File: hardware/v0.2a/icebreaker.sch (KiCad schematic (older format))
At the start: 114 parts, among them J1 Jumper, J10 Jumper, J11 Jumper, J12 Jumper, J13 Jumper, J14 Jumper, J15 Jumper, J16 Jumper, J17 Jumper, J18 Jumper, J19 Jumper, J2 Jumper, J20 Flash, J21 PMOD_1A, J22 PMOD_1B, J23 PMOD_2H, J24 PMOD_2P, J25 RGB Led, J26 5V AUX, J27 5V AUX, J3 Jumper, J4 Jumper, J5 Jumper, J6 Jumper, J7 Jumper, J8 Jumper, J9 Jumper, P1 pkl_USB_OTG, SW1 TACT, SW2 TACT, SW3 TACT, SW4 TACT, U1 93C46B-SOT-23-6, U2 3.3V, U3 1V2, U4 FT2232H, U5 W25Q, U6 ICE5LP4K-SG48, U7 12MHz

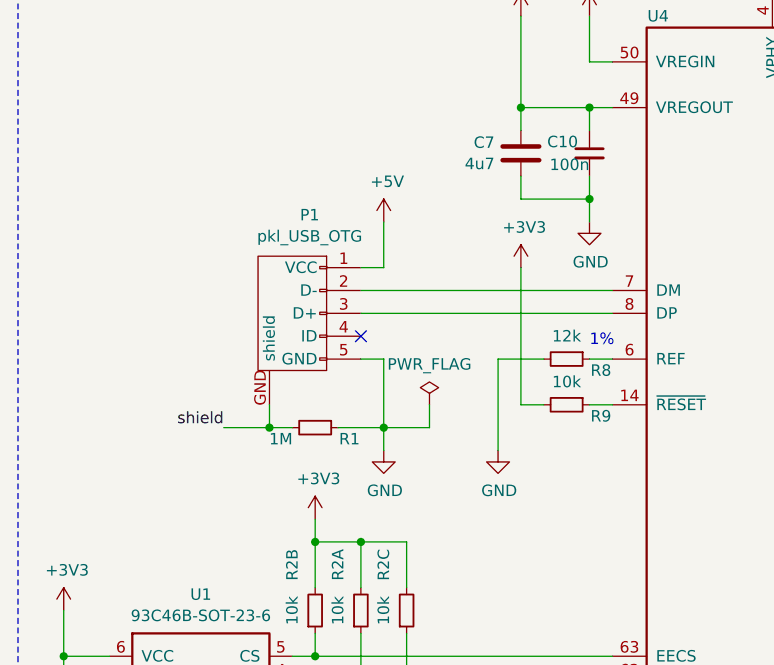
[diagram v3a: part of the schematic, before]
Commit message: Added USB signal pads.
These pads can be used for testing, debugging as well as hard wiring a
usb extension cable.
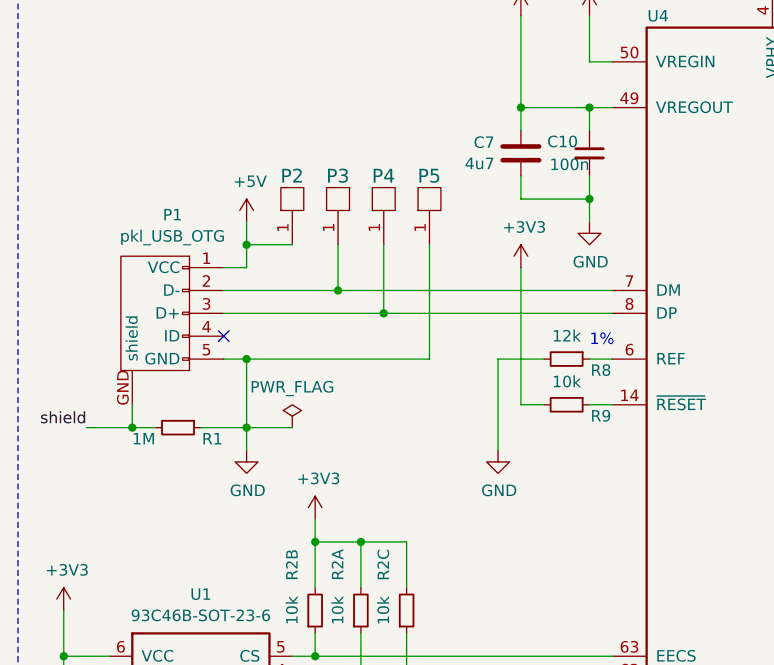
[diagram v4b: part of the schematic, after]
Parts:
- added P2, P3, P4, P5: UP, pkl_pads:PAD_SMD_1x2.65, symbol pkl_misc:PAD_SMD
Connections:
- net +5V: now also P2.1 (PAD)
- net GND: now also P5.1 (PAD)
- net at P1.2 (D-), U4.7 (DM): now also P3.1 (PAD)
- net at P1.3 (D+), U4.8 (DP): now also P4.1 (PAD)
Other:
- moved on the sheet: P1, R1
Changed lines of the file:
@@
 L pkl_conn:pkl_USB_OTG P1
 U 1 1 5A52ACD0
-P 1700 4350
-F 0 "P1" V 1270 4274 50  0000 C CNN
-F 1 "pkl_USB_OTG" V 1363 4274 50  0000 C CNN
-F 2 "pkl_connectors:Connector_USB_Micro_B_SMD" V 1355 4274 60  0001 C CNN
-F 3 "" V 1650 4250 60  0000 C CNN
-F 4 "ANY" H 1700 4350 50  0001 C CNN "Source"
-F 5 "conn-smd-usb-micro-b" H 0   0   50  0001 C CNN "Key"
-	1    1700 4350
+P 1100 4350
+F 0 "P1" V 670 4274 50  0000 C CNN
+F 1 "pkl_USB_OTG" V 763 4274 50  0000 C CNN
+F 2 "pkl_connectors:Connector_USB_Micro_B_SMD" V 755 4274 60  0001 C CNN
+F 3 "" V 1050 4250 60  0000 C CNN
+F 4 "ANY" H 1100 4350 50  0001 C CNN "Source"
+F 5 "conn-smd-usb-micro-b" H -600 0   50  0001 C CNN "Key"
+	1    1100 4350
 	0    -1   1    0
 $EndComp
 Wire Wire Line
-	2000 4250 3100 4250
+	1400 4250 1900 4250
 Wire Wire Line
-	2000 4350 3100 4350
-NoConn ~ 2000 4450
+	1400 4350 2100 4350
+NoConn ~ 1400 4450
 Wire Wire Line
-	2000 4550 2100 4550
+	1400 4550 1500 4550
 Wire Wire Line
-	2100 4550 2100 4850
+	1500 4550 1500 4850
 Wire Wire Line
-	1600 4750 1600 4850
+	1000 4750 1000 4850
 Wire Wire Line
-	1600 4850 1400 4850
-Text Label 1400 4850 2    50   ~ 0
+	1000 4850 800  4850
+Text Label 800  4850 2    50   ~ 0
 shield
 $Comp
 L pkl_device:pkl_R_Small R1
 U 1 1 5A52EC58
-P 1800 4850
-F 0 "R1" V 1850 5000 50  0000 C CNN
-F 1 "1M" V 1850 4700 50  0000 C CNN
-F 2 "pkl_dipol:R_0402" H 1859 4757 60  0001 L CNN
-F 3 "" H 1800 4850 60  0000 C CNN
-F 4 "ANY" H 1800 4850 50  0001 C CNN "Source"
-F 5 "res-0402-1m" H 0   0   50  0001 C CNN "Key"
-	1    1800 4850
+P 1200 4850
+F 0 "R1" V 1250 5000 50  0000 C CNN
+F 1 "1M" V 1250 4700 50  0000 C CNN
+F 2 "pkl_dipol:R_0402" H 1259 4757 60  0001 L CNN
+F 3 "" H 1200 4850 60  0000 C CNN
+F 4 "ANY" H 1200 4850 50  0001 C CNN "Source"
+F 5 "res-0402-1m" H -600 0   50  0001 C CNN "Key"
+	1    1200 4850
 	0    1    1    0
 $EndComp
 Wire Wire Line
-	1600 4850 1700 4850
-Connection ~ 1600 4850
+	1000 4850 1100 4850
+Connection ~ 1000 4850
 Wire Wire Line
-	1900 4850 2100 4850
+	1300 4850 1500 4850
 Wire Wire Line
-	2100 4850 2100 4950
-Connection ~ 2100 4850
+	1500 4850 1500 4950
+Connection ~ 1500 4850
 $Comp
 L power:GND #PWR06
 U 1 1 5A530D58
-P 2100 4950
-F 0 "#PWR06" H 2100 4700 50  0001 C CNN
-F 1 "GND" H 2105 4774 50  0000 C CNN
-F 2 "" H 2100 4950 50  0001 C CNN
-F 3 "" H 2100 4950 50  0001 C CNN
-	1    2100 4950
+P 1500 4950
+F 0 "#PWR06" H 1500 4700 50  0001 C CNN
+F 1 "GND" H 1505 4774 50  0000 C CNN
+F 2 "" H 1500 4950 50  0001 C CNN
+F 3 "" H 1500 4950 50  0001 C CNN
+	1    1500 4950
 	1    0    0    -1
 $EndComp
@@
 L power:PWR_FLAG #FLG01
 U 1 1 5A530EEE
-P 2300 4750
-F 0 "#FLG01" H 2300 4825 50  0001 C CNN
-F 1 "PWR_FLAG" H 2300 4927 50  0000 C CNN
-F 2 "" H 2300 4750 50  0001 C CNN
-F 3 "" H 2300 4750 50  0001 C CNN
-	1    2300 4750
+P 1700 4850
+F 0 "#FLG01" H 1700 4925 50  0001 C CNN
+F 1 "PWR_FLAG" H 1700 5027 50  0000 C CNN
+F 2 "" H 1700 4850 50  0001 C CNN
+F 3 "" H 1700 4850 50  0001 C CNN
+	1    1700 4850
 	1    0    0    -1
 $EndComp
 Wire Wire Line
-	2100 4850 2300 4850
-Wire Wire Line
-	2300 4850 2300 4750
+	1500 4850 1700 4850
 Wire Wire Line
 	3100 3250 3000 3250
@@
 $EndComp
 Wire Wire Line
-	2000 4150 2100 4150
-Wire Wire Line
-	2100 4150 2100 3950
+	1400 4150 1500 4150
 $Comp
 L power:+5V #PWR08
 U 1 1 5A5336DE
-P 2100 3950
-F 0 "#PWR08" H 2100 3800 50  0001 C CNN
-F 1 "+5V" H 2115 4126 50  0000 C CNN
-F 2 "" H 2100 3950 50  0001 C CNN
-F 3 "" H 2100 3950 50  0001 C CNN
-	1    2100 3950
+P 1500 3950
+F 0 "#PWR08" H 1500 3800 50  0001 C CNN
+F 1 "+5V" H 1515 4126 50  0000 C CNN
+F 2 "" H 1500 3950 50  0001 C CNN
+F 3 "" H 1500 3950 50  0001 C CNN
+	1    1500 3950
 	1    0    0    -1
 $EndComp
@@
 Text Label 12500 5700 2    25   ~ 0
 P2_4x
+$Comp
+L pkl_misc:PAD_SMD P2
+U 1 1 5D27BE59
+P 1700 3850
+F 0 "P2" V 1800 3800 60  0000 L CNN
+F 1 "UP" H 1650 3950 60  0001 L CNN
+F 2 "pkl_pads:PAD_SMD_1x2.65" H 1700 3600 60  0001 C CNN
+F 3 "" H 1700 3700 60  0000 C CNN
+F 4 "ANY" H 1700 3850 50  0001 C CNN "Source"
+	1    1700 3850
+	0    -1   -1   0
+$EndComp
+Connection ~ 1900 4250
+Wire Wire Line
+	1900 4250 3100 4250
+Wire Wire Line
+	1900 4050 1900 4250
+Wire Wire Line
+	1500 3950 1500 4050
+Wire Wire Line
+	1700 4050 1500 4050
+Connection ~ 1500 4050
+Wire Wire Line
+	1500 4050 1500 4150
+Wire Wire Line
+	2100 4050 2100 4350
+Connection ~ 2100 4350
+Wire Wire Line
+	2100 4350 3100 4350
+Wire Wire Line
+	2300 4050 2300 4550
+Wire Wire Line
+	2300 4550 1500 4550
+Connection ~ 1500 4550
+$Comp
+L pkl_misc:PAD_SMD P3
+U 1 1 5D620E4E
+P 1900 3850
+F 0 "P3" V 2000 3800 60  0000 L CNN
+F 1 "UP" H 1850 3950 60  0001 L CNN
+F 2 "pkl_pads:PAD_SMD_1x2.65" H 1900 3600 60  0001 C CNN
+F 3 "" H 1900 3700 60  0000 C CNN
+F 4 "ANY" H 1900 3850 50  0001 C CNN "Source"
+	1    1900 3850
+	0    -1   -1   0
+$EndComp
+$Comp
+L pkl_misc:PAD_SMD P4
+U 1 1 5D620F84
+P 2100 3850
+F 0 "P4" V 2200 3800 60  0000 L CNN
+F 1 "UP" H 2050 3950 60  0001 L CNN
+F 2 "pkl_pads:PAD_SMD_1x2.65" H 2100 3600 60  0001 C CNN
+F 3 "" H 2100 3700 60  0000 C CNN
+F 4 "ANY" H 2100 3850 50  0001 C CNN "Source"
+	1    2100 3850
+	0    -1   -1   0
+$EndComp
+$Comp
+L pkl_misc:PAD_SMD P5
+U 1 1 5D6210C0
+P 2300 3850
+F 0 "P5" V 2400 3800 60  0000 L CNN
+F 1 "UP" H 2250 3950 60  0001 L CNN
+F 2 "pkl_pads:PAD_SMD_1x2.65" H 2300 3600 60  0001 C CNN
+F 3 "" H 2300 3700 60  0000 C CNN
+F 4 "ANY" H 2300 3850 50  0001 C CNN "Source"
+	1    2300 3850
+	0    -1   -1   0
+$EndComp
 $EndSCHEMATC

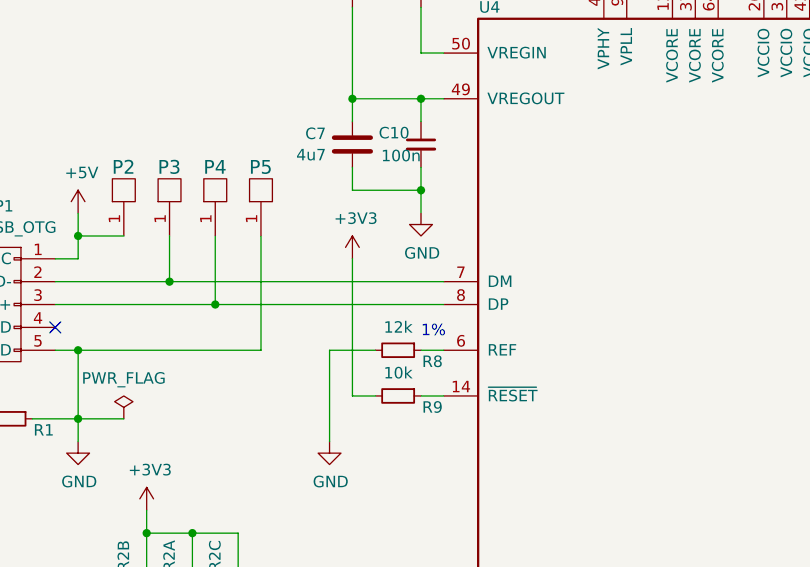
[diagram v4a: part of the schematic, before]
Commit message: Improved silkscreen legend for more intutive usage.
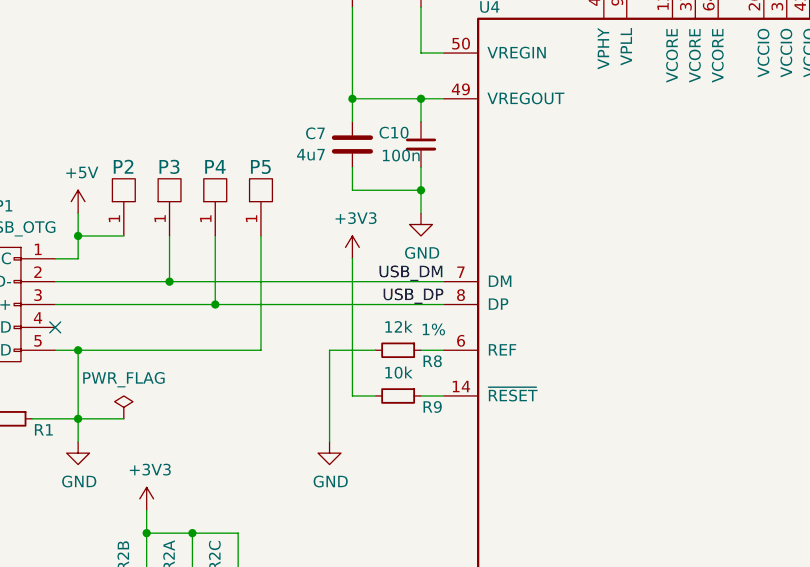
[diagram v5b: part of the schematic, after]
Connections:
- net USB_DM: now reaches P1.2 (D-), P3.1 (PAD), U4.7 (DM)
- net USB_DP: now reaches P1.3 (D+), P4.1 (PAD), U4.8 (DP)
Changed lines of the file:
@@
 	0    -1   -1   0
 $EndComp
+Text Label 3100 4250 2    50   ~ 0
+USB_DM
+Text Label 3100 4350 2    50   ~ 0
+USB_DP
 $EndSCHEMATC

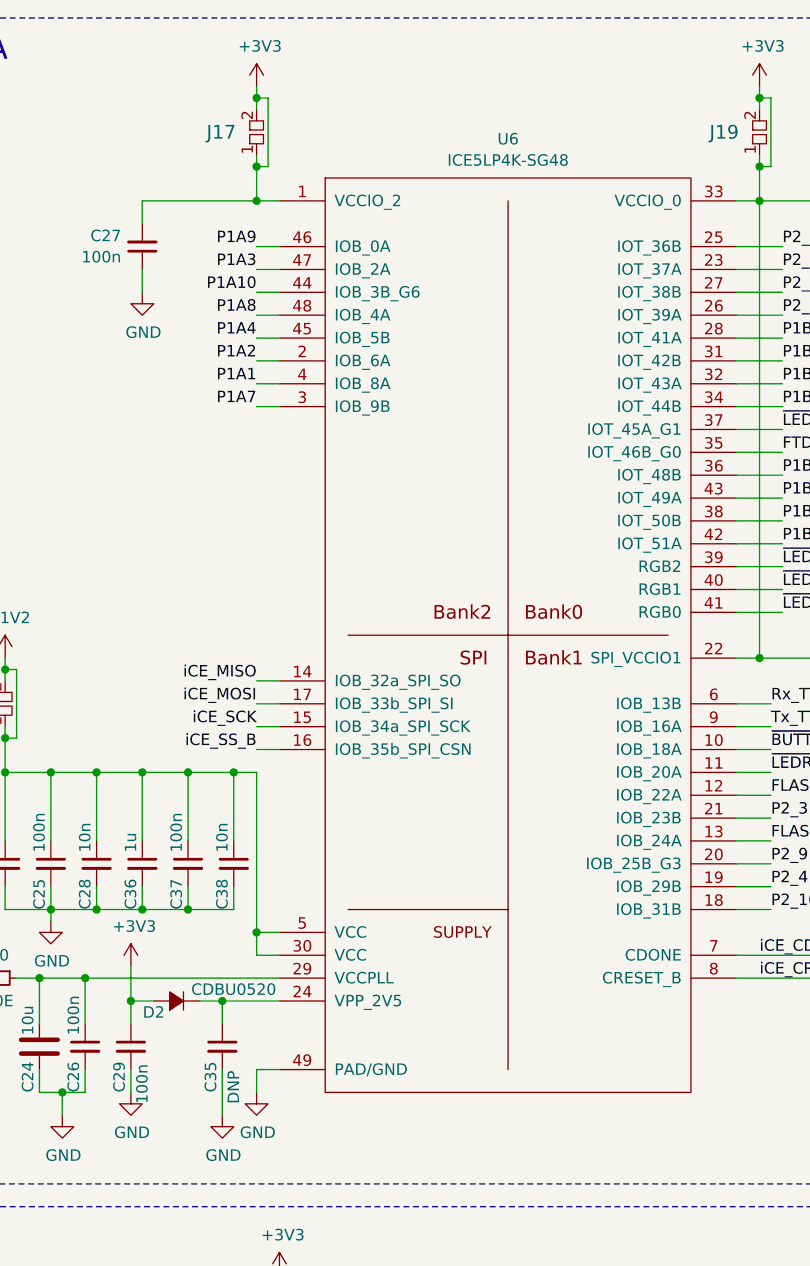
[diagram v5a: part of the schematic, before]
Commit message: Fixed pin header 3d models.
We had some of the models doubled up or not fully disabled. Now the TH
pin headers are all using KiCad V5 3d model locations and are all
disabled.

This fixes #23
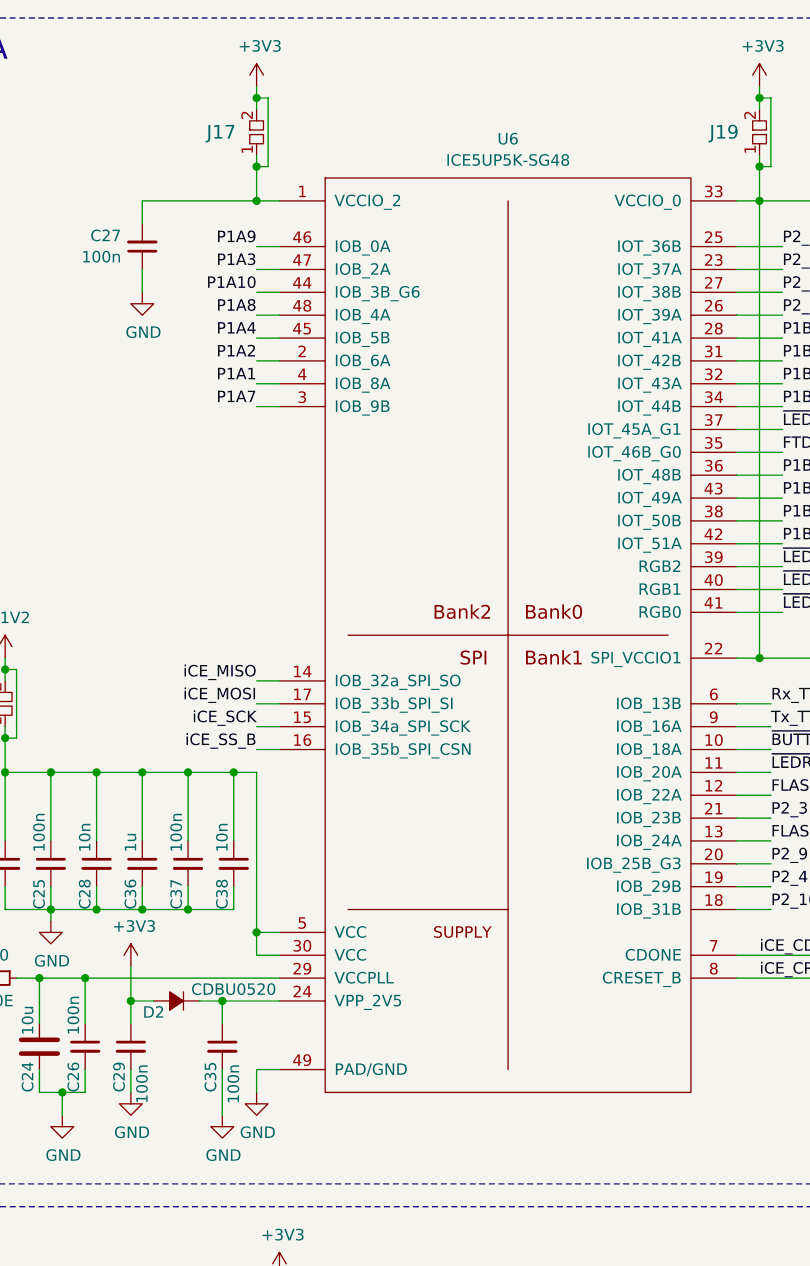
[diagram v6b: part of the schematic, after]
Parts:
- C35: value DNP -> 100n; Key (none) -> cap-cer-100n
- C6, C7, C9: Key cap-cer-0402-4u7 -> cap-cer-0603-4u7
- D2: Key diode-shottky-0603 -> diode-schottky-0603
- U6: value ICE5LP4K-SG48 -> ICE5UP5K-SG48; Key ic-ice5lp4k-sg48 -> ic-ice5up5k-sg48
- U7: Key (none) -> xtal-sot23-5-12mhz-osc
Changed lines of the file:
@@
 P 9600 4200
 F 0 "U6" H 9600 6370 50  0000 C CNN
-F 1 "ICE5LP4K-SG48" H 9600 6277 50  0000 C CNN
+F 1 "ICE5UP5K-SG48" H 9600 6277 50  0000 C CNN
 F 2 "pkl_housings_dfn_qfn:QFN-48-1EP_7x7mm_Pitch0.5mm" H 11900 4400 50  0001 C CNN
 F 3 "" H 11900 4400 50  0001 C CNN
-F 4 "ANY" H 9600 4200 50  0001 C CNN "Source"
-F 5 "ic-ice5lp4k-sg48" H 0   0   50  0001 C CNN "Key"
+F 4 "ic-ice5up5k-sg48" H 0   0   50  0001 C CNN "Key"
+F 5 "ANY" H 9600 4200 50  0001 C CNN "Source"
 	1    9600 4200
 	1    0    0    -1
@@
 F 2 "pkl_dipol:C_0603" H 3092 2357 60  0001 L CNN
 F 3 "" H 3000 2450 60  0000 C CNN
-F 4 "cap-cer-0402-4u7" H 0   0   50  0001 C CNN "Key"
+F 4 "cap-cer-0603-4u7" H 0   0   50  0001 C CNN "Key"
 F 5 "ANY" H 3000 2450 50  0001 C CNN "Source"
 	1    3000 2450
@@
 F 2 "pkl_dipol:C_0603" H 2792 2357 60  0001 L CNN
 F 3 "" H 2700 2450 60  0000 C CNN
-F 4 "cap-cer-0402-4u7" H 0   0   50  0001 C CNN "Key"
+F 4 "cap-cer-0603-4u7" H 0   0   50  0001 C CNN "Key"
 F 5 "ANY" H 2700 2450 50  0001 C CNN "Source"
 	1    2700 2450
@@
 F 2 "pkl_dipol:D_0603" V 8150 5800 60  0001 C CNN
 F 3 "" V 8150 5800 60  0000 C CNN
-F 4 "ANY" H 8150 5800 50  0001 C CNN "Source"
-F 5 "diode-shottky-0603" H 0   0   50  0001 C CNN "Key"
+F 4 "diode-schottky-0603" H 0   0   50  0001 C CNN "Key"
+F 5 "ANY" H 8150 5800 50  0001 C CNN "Source"
 	1    8150 5800
 	1    0    0    -1
@@
 F 2 "pkl_dipol:C_0603" H 2792 3557 60  0001 L CNN
 F 3 "" H 2700 3650 60  0000 C CNN
-F 4 "cap-cer-0402-4u7" H 0   0   50  0001 C CNN "Key"
+F 4 "cap-cer-0603-4u7" H 0   0   50  0001 C CNN "Key"
 F 5 "ANY" H 2700 3650 50  0001 C CNN "Source"
 	1    2700 3650
@@
 P 8350 6000
 F 0 "C35" V 8400 5800 50  0000 L CNN
-F 1 "DNP" V 8300 5750 50  0000 L CNN
+F 1 "100n" V 8300 5750 50  0000 L CNN
 F 2 "pkl_dipol:C_0402" H 8442 5907 60  0001 L CNN
 F 3 "" H 8350 6000 60  0000 C CNN
-F 4 "ANY" H 8350 6000 50  0001 C CNN "Source"
+F 4 "cap-cer-100n" H 8350 6000 50  0001 C CNN "Key"
+F 5 "ANY" H 8350 6000 50  0001 C CNN "Source"
 	1    8350 6000
 	-1   0    0    -1
@@
 F 2 "pkl_housings_sot:SOT-23-5" H 2000 6700 50  0001 C CNN
 F 3 "" H 2000 6700 50  0001 C CNN
-F 4 "ANY" H 2000 6800 50  0001 C CNN "Source"
+F 4 "xtal-sot23-5-12mhz-osc" H 2000 6800 50  0001 C CNN "Key"
+F 5 "ANY" H 2000 6800 50  0001 C CNN "Source"
 	1    2000 6800
 	-1   0    0    -1
